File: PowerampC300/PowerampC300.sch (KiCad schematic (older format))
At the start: 95 parts, among them J1 Conn_01x02, J2 Conn_01x02, J3 Conn_01x02, J4 Conn_01x01, J5 Conn_01x01, J6 Conn_01x01, J7 Conn_01x01, J8 Conn_01x02, J9 Conn_Coaxial, Q1 BC546, Q10 MJE350, Q11 MJE340, Q12 MJE340, Q13 BC546, Q14 BC556, Q15 MJE340, Q16 MJE350, Q17 MJL3281A, Q18 MJL1302A, Q19 MJL3281A, Q2 BC546, Q20 MJL1302A, Q21 MJL3281A, Q22 MJL1302A, Q23 MJL3281A, Q24 MJL1302A, Q3 BC556, Q4 BC556, Q5 BC546, Q6 BC546, Q7 BC546, Q8 MPSA92, Q9 BC556

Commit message: Added credit where credit is due
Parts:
- added C16, C17, C18, C19: 100 uF, Capacitors_THT:CP_Radial_D14.0mm_P7.50mm, symbol CP_Small
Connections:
- net +48V: now also C16.1, C17.1
- net -48V: now also C18.2, C19.2
- net GND: now also C16.2, C17.2, C18.1, C19.1
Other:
- note added: "c300 Designed by Michael Chua (AmpsLab)\nPCB and modifications by Daniel Marks CC-BY-SA 4.0"
- note removed: "C300 Audio Amplifier by Michael Chua\nPCB and modifications by Daniel Marks CC-BY-SA 4.0"
- moved on the sheet: C11, C14, C15, J1, J4, J5, J6, J7, J8, J9, R41

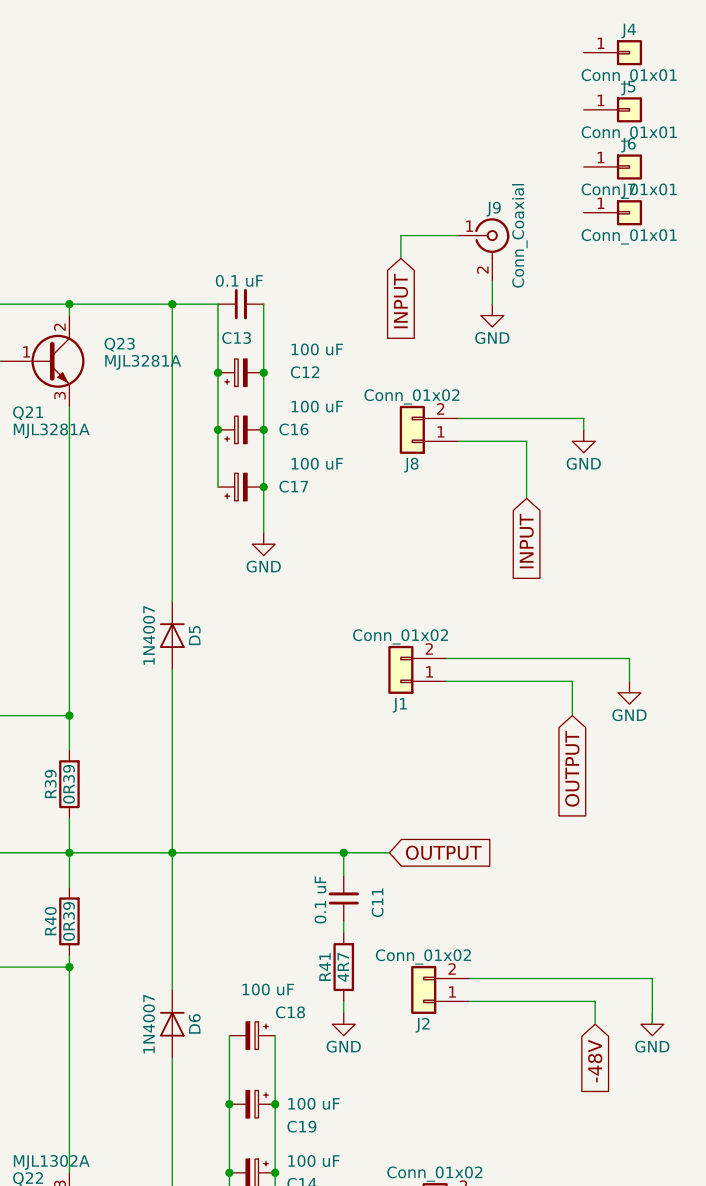
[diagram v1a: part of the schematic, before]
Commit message: Added soft start circuit
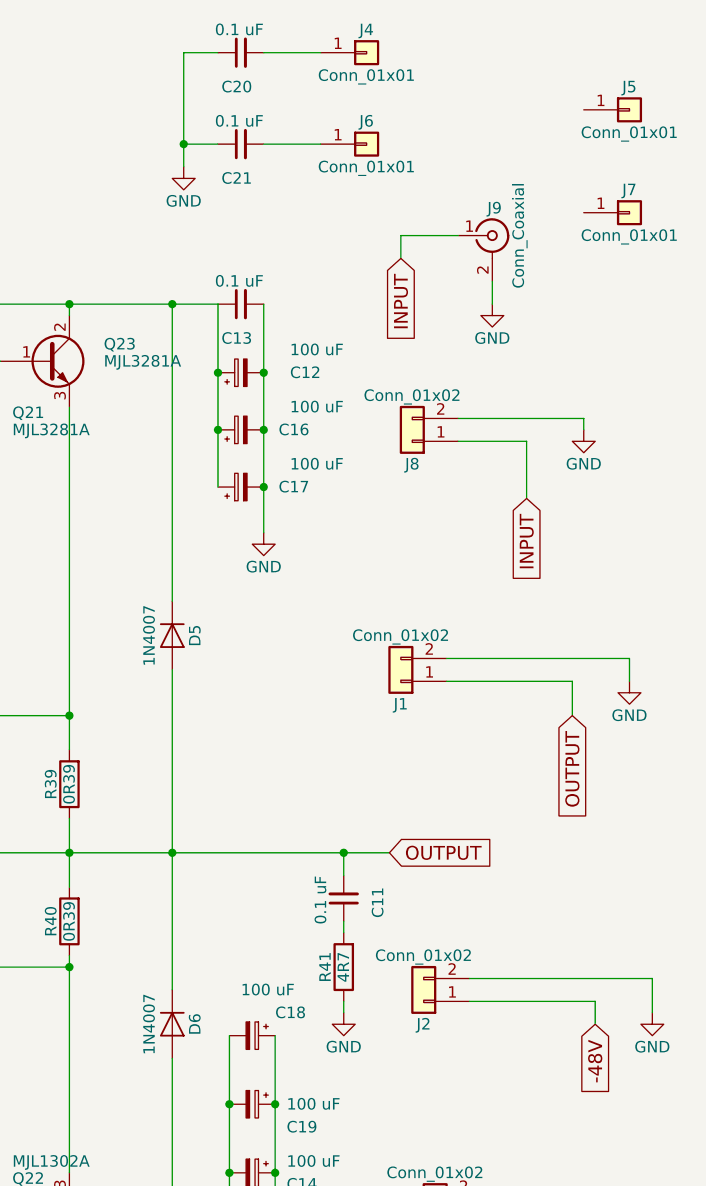
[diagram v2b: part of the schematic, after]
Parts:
- added C20, C21: 0.1 uF, Capacitors_THT:C_Disc_D5.0mm_W2.5mm_P5.00mm, symbol C_Small
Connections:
- net GND: now also J2.2 (Pin_2), C20.1, C21.1
- net at J4.1 (Pin_1): now also C20.2
- net at J6.1 (Pin_1): now also C21.2
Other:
- moved on the sheet: J4, J6
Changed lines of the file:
@@
 $EndComp
 $Comp
-L GND #PWR01
+L GND #PWR2
 U 1 1 5F3B0902
 P 1000 4100
-F 0 "#PWR01" H 1000 3850 50  0001 C CNN
+F 0 "#PWR2" H 1000 3850 50  0001 C CNN
 F 1 "GND" H 1000 3950 50  0000 C CNN
 F 2 "" H 1000 4100 50  0001 C CNN
@@
 $EndComp
 $Comp
-L GND #PWR02
+L GND #PWR4
 U 1 1 5F3B09D1
 P 1500 4100
-F 0 "#PWR02" H 1500 3850 50  0001 C CNN
+F 0 "#PWR4" H 1500 3850 50  0001 C CNN
 F 1 "GND" H 1500 3950 50  0000 C CNN
 F 2 "" H 1500 4100 50  0001 C CNN
@@
 $EndComp
 $Comp
-L GND #PWR03
+L GND #PWR1
 U 1 1 5F3B1EB5
 P 950 3400
-F 0 "#PWR03" H 950 3150 50  0001 C CNN
+F 0 "#PWR1" H 950 3150 50  0001 C CNN
 F 1 "GND" H 950 3250 50  0000 C CNN
 F 2 "" H 950 3400 50  0001 C CNN
@@
 $EndComp
 $Comp
-L GND #PWR04
+L GND #PWR3
 U 1 1 5F3B1F70
 P 1300 3400
-F 0 "#PWR04" H 1300 3150 50  0001 C CNN
+F 0 "#PWR3" H 1300 3150 50  0001 C CNN
 F 1 "GND" H 1300 3250 50  0000 C CNN
 F 2 "" H 1300 3400 50  0001 C CNN
@@
 $EndComp
 $Comp
-L GND #PWR05
+L GND #PWR5
 U 1 1 5F3B40A9
 P 3000 4750
-F 0 "#PWR05" H 3000 4500 50  0001 C CNN
+F 0 "#PWR5" H 3000 4500 50  0001 C CNN
 F 1 "GND" H 3000 4600 50  0000 C CNN
 F 2 "" H 3000 4750 50  0001 C CNN
@@
 $EndComp
 $Comp
-L GND #PWR06
+L GND #PWR6
 U 1 1 5F3B638D
 P 3100 3000
-F 0 "#PWR06" H 3100 2750 50  0001 C CNN
+F 0 "#PWR6" H 3100 2750 50  0001 C CNN
 F 1 "GND" H 3100 2850 50  0000 C CNN
 F 2 "" H 3100 3000 50  0001 C CNN
@@
 $EndComp
 $Comp
-L GND #PWR07
+L GND #PWR10
 U 1 1 5F3C725A
 P 9450 4900
-F 0 "#PWR07" H 9450 4650 50  0001 C CNN
+F 0 "#PWR10" H 9450 4650 50  0001 C CNN
 F 1 "GND" H 9450 4750 50  0000 C CNN
 F 2 "" H 9450 4900 50  0001 C CNN
@@
 $EndComp
 $Comp
-L GND #PWR08
+L GND #PWR9
 U 1 1 5F3C82FF
 P 9150 6100
-F 0 "#PWR08" H 9150 5850 50  0001 C CNN
+F 0 "#PWR9" H 9150 5850 50  0001 C CNN
 F 1 "GND" H 9150 5950 50  0000 C CNN
 F 2 "" H 9150 6100 50  0001 C CNN
@@
 $EndComp
 $Comp
-L GND #PWR09
+L GND #PWR8
 U 1 1 5F3C9FC4
 P 9100 2800
-F 0 "#PWR09" H 9100 2550 50  0001 C CNN
+F 0 "#PWR8" H 9100 2550 50  0001 C CNN
 F 1 "GND" H 9100 2650 50  0000 C CNN
 F 2 "" H 9100 2800 50  0001 C CNN
@@
 OUTPUT
 $Comp
-L GND #PWR010
+L GND #PWR14
 U 1 1 5F3D5C64
 P 10700 3450
-F 0 "#PWR010" H 10700 3200 50  0001 C CNN
+F 0 "#PWR14" H 10700 3200 50  0001 C CNN
 F 1 "GND" H 10700 3300 50  0000 C CNN
 F 2 "" H 10700 3450 50  0001 C CNN
@@
 $EndComp
 $Comp
-L GND #PWR011
+L GND #PWR13
 U 1 1 5F3D7497
 P 10650 5700
-F 0 "#PWR011" H 10650 5450 50  0001 C CNN
+F 0 "#PWR13" H 10650 5450 50  0001 C CNN
 F 1 "GND" H 10650 5550 50  0000 C CNN
 F 2 "" H 10650 5700 50  0001 C CNN
@@
 $EndComp
 $Comp
-L GND #PWR012
+L GND #PWR15
 U 1 1 5F3D76F6
 P 10800 4900
-F 0 "#PWR012" H 10800 4650 50  0001 C CNN
+F 0 "#PWR15" H 10800 4650 50  0001 C CNN
 F 1 "GND" H 10800 4750 50  0000 C CNN
 F 2 "" H 10800 4900 50  0001 C CNN
@@
 L Conn_01x01 J4
 U 1 1 5F3DDB47
-P 10700 700
-F 0 "J4" H 10700 800 50  0000 C CNN
-F 1 "Conn_01x01" H 10700 600 50  0000 C CNN
-F 2 "Connectors:1pin" H 10700 700 50  0001 C CNN
-F 3 "" H 10700 700 50  0001 C CNN
-	1    10700 700
+P 9550 700
+F 0 "J4" H 9550 800 50  0000 C CNN
+F 1 "Conn_01x01" H 9550 600 50  0000 C CNN
+F 2 "Connectors:1pin" H 9550 700 50  0001 C CNN
+F 3 "" H 9550 700 50  0001 C CNN
+	1    9550 700
 	1    0    0    -1
 $EndComp
@@
 L Conn_01x01 J6
 U 1 1 5F3DDEAC
-P 10700 1200
-F 0 "J6" H 10700 1300 50  0000 C CNN
-F 1 "Conn_01x01" H 10700 1100 50  0000 C CNN
-F 2 "Connectors:1pin" H 10700 1200 50  0001 C CNN
-F 3 "" H 10700 1200 50  0001 C CNN
-	1    10700 1200
+P 9550 1100
+F 0 "J6" H 9550 1200 50  0000 C CNN
+F 1 "Conn_01x01" H 9550 1000 50  0000 C CNN
+F 2 "Connectors:1pin" H 9550 1100 50  0001 C CNN
+F 3 "" H 9550 1100 50  0001 C CNN
+	1    9550 1100
 	1    0    0    -1
 $EndComp
@@
 $EndComp
 $Comp
-L GND #PWR013
+L GND #PWR12
 U 1 1 5F3DED23
 P 10500 2350
-F 0 "#PWR013" H 10500 2100 50  0001 C CNN
+F 0 "#PWR12" H 10500 2100 50  0001 C CNN
 F 1 "GND" H 10500 2200 50  0000 C CNN
 F 2 "" H 10500 2350 50  0001 C CNN
@@
 INPUT
 $Comp
-L GND #PWR014
+L GND #PWR11
 U 1 1 5F3DF546
 P 10100 1800
-F 0 "#PWR014" H 10100 1550 50  0001 C CNN
+F 0 "#PWR11" H 10100 1550 50  0001 C CNN
 F 1 "GND" H 10100 1650 50  0000 C CNN
 F 2 "" H 10100 1800 50  0001 C CNN
@@
 	10500 5800 10500 5900
 Wire Wire Line
-	10800 4750 10800 4950
-Wire Wire Line
 	4750 3500 4200 3500
 Connection ~ 4200 3500
@@
 Connection ~ 8950 5600
 Connection ~ 8950 5300
+$Comp
+L C_Small C20
+U 1 1 5F400E18
+P 9000 700
+F 0 "C20" V 8850 650 50  0000 L CNN
+F 1 "0.1 uF" V 9100 600 50  0000 L CNN
+F 2 "Capacitors_THT:C_Disc_D5.0mm_W2.5mm_P5.00mm" H 9000 700 50  0001 C CNN
+F 3 "" H 9000 700 50  0001 C CNN
+	1    9000 700
+	0    -1   -1   0
+$EndComp
+Wire Wire Line
+	9350 700  9100 700
+$Comp
+L C_Small C21
+U 1 1 5F40170E
+P 9000 1100
+F 0 "C21" V 8850 1050 50  0000 L CNN
+F 1 "0.1 uF" V 9100 1000 50  0000 L CNN
+F 2 "Capacitors_THT:C_Disc_D5.0mm_W2.5mm_P5.00mm" H 9000 1100 50  0001 C CNN
+F 3 "" H 9000 1100 50  0001 C CNN
+	1    9000 1100
+	0    -1   -1   0
+$EndComp
+Wire Wire Line
+	9350 1100 9100 1100
+$Comp
+L GND #PWR7
+U 1 1 5F401BCA
+P 8750 1200
+F 0 "#PWR7" H 8750 950 50  0001 C CNN
+F 1 "GND" H 8750 1050 50  0000 C CNN
+F 2 "" H 8750 1200 50  0001 C CNN
+F 3 "" H 8750 1200 50  0001 C CNN
+	1    8750 1200
+	1    0    0    -1
+$EndComp
+Wire Wire Line
+	8750 700  8750 1200
+Wire Wire Line
+	8750 700  8900 700
+Wire Wire Line
+	8900 1100 8750 1100
+Connection ~ 8750 1100
+Wire Wire Line
+	10800 4750 10800 4900
 $EndSCHEMATC

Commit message: Submitted to JLCPCB 2020-08-24
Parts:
- C1: footprint Capacitors_THT:C_Axial_L5.1mm_D3.1mm_P10.00mm_Horizontal -> Capacitors_THT:C_Rect_L16.5mm_W5.0mm_P15.00mm_MKT; LCSC (none) -> C328801
- C10, C11, C13, C15: LCSC (none) -> C390130
- C12, C14, C16, C17, C18, C19: LCSC (none) -> C330940
- C2: LCSC (none) -> C328872
- C3: LCSC (none) -> C434407
- C4, C5: LCSC (none) -> C454377
- C6: LCSC (none) -> C342428
- C7, C8: LCSC (none) -> C88750
- C9: LCSC (none) -> C366798
- D1: value 1N4477 -> 1N4752A; LCSC (none) -> C2555
- D2: LCSC (none) -> C99771
- D3, D4: LCSC (none) -> C125770
- D5, D6: LCSC (none) -> C193790
- J1, J2, J3, J8: LCSC (none) -> C395849
- J9: LCSC (none) -> C496549
- Q1, Q12, Q13, Q2, Q5, Q6, Q7: LCSC (none) -> C142464
- Q10, Q16: LCSC (none) -> C283403
- Q11, Q15: LCSC (none) -> C283424
- Q14, Q3, Q4, Q9: LCSC (none) -> C305414
- Q17, Q19, Q23: LCSC (none) -> C327498
- Q18, Q20, Q22, Q24: LCSC (none) -> C327497
- Q21: LCSC' (none) -> C327498
- Q8: LCSC (none) -> C305412
- R1, R17: LCSC (none) -> C57435
- R10: LCSC (none) -> C83688
- R11, R16: LCSC (none) -> C176446
- R12: LCSC (none) -> C58613
- R13: LCSC (none) -> C138185
- R14, R2: LCSC (none) -> C57436
- R15, R18: LCSC (none) -> C58608
- R19: LCSC (none) -> C176452
- R20: LCSC (none) -> C176487
- R21: LCSC (none) -> C173010
- R22: LCSC (none) -> C83685
- R23: LCSC (none) -> C172973
- R24, R8, R9: LCSC (none) -> C119298
- R25, R28: LCSC (none) -> C138189
- R26, R27, R31, R32: LCSC (none) -> C173006
- R29, R30: LCSC (none) -> C172969
- R3, R4: LCSC (none) -> C172976
- R33, R34, R35, R36, R37, R38, R39, R40: LCSC (none) -> C334290
- R41: LCSC (none) -> C57725
- R5: LCSC (none) -> C173036
- R6, R7: LCSC (none) -> C172966
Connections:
- net GND: now also Q8.3 (C); no longer Q8.1 (E)
- net at Q10.3 (B), Q9.1 (C), R17.1: now also Q8.1 (E); no longer Q8.3 (C)
